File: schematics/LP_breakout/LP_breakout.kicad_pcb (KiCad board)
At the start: 2 copper layers, 39.8 x 69.8 mm, 8 parts, among them J1 RJ45, J2 Conn_01x03_Socket, J3 Conn_02x04_Odd_Even, J4 Conn_02x15_Odd_Even, J5 Conn_02x02_Odd_Even, J6 Conn_01x03_Socket, J7 Conn_01x03_Socket, J8 Conn_01x03_Socket

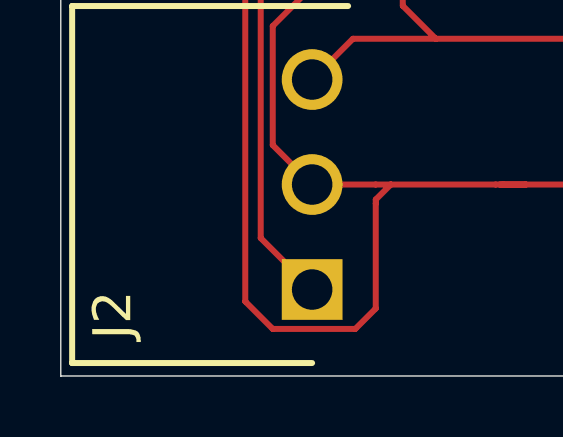
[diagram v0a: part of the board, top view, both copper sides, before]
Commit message: Updated LP Breakout for JLC
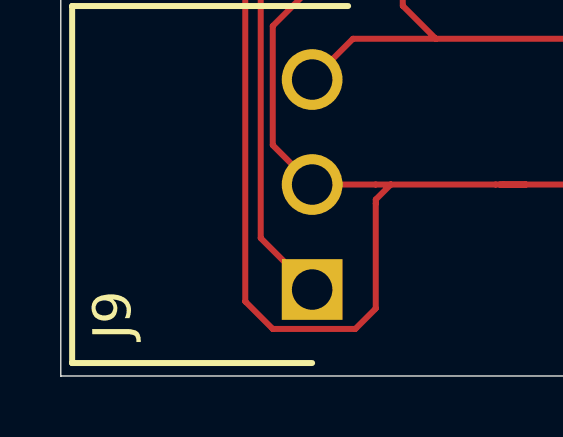
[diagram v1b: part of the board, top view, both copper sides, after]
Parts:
- renumbered J2 to J9
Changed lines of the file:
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@@
 			(drillshape 0)
 			(scaleselection 1)
-			(outputdirectory "./")
+			(outputdirectory "C:/Users/smbea/OneDrive/Personal_Files/School/Fall_2025/OATS/avena-rs/schematics/LP_breakout/JLCPCB/")
 		)
 	)
@@
 		(descr "1844223")
 		(tags "Connector")
-		(property "Reference" "J2"
+		(property "Reference" "J9"
 			(at -0.849 -6.65 90)
 			(layer "F.SilkS")

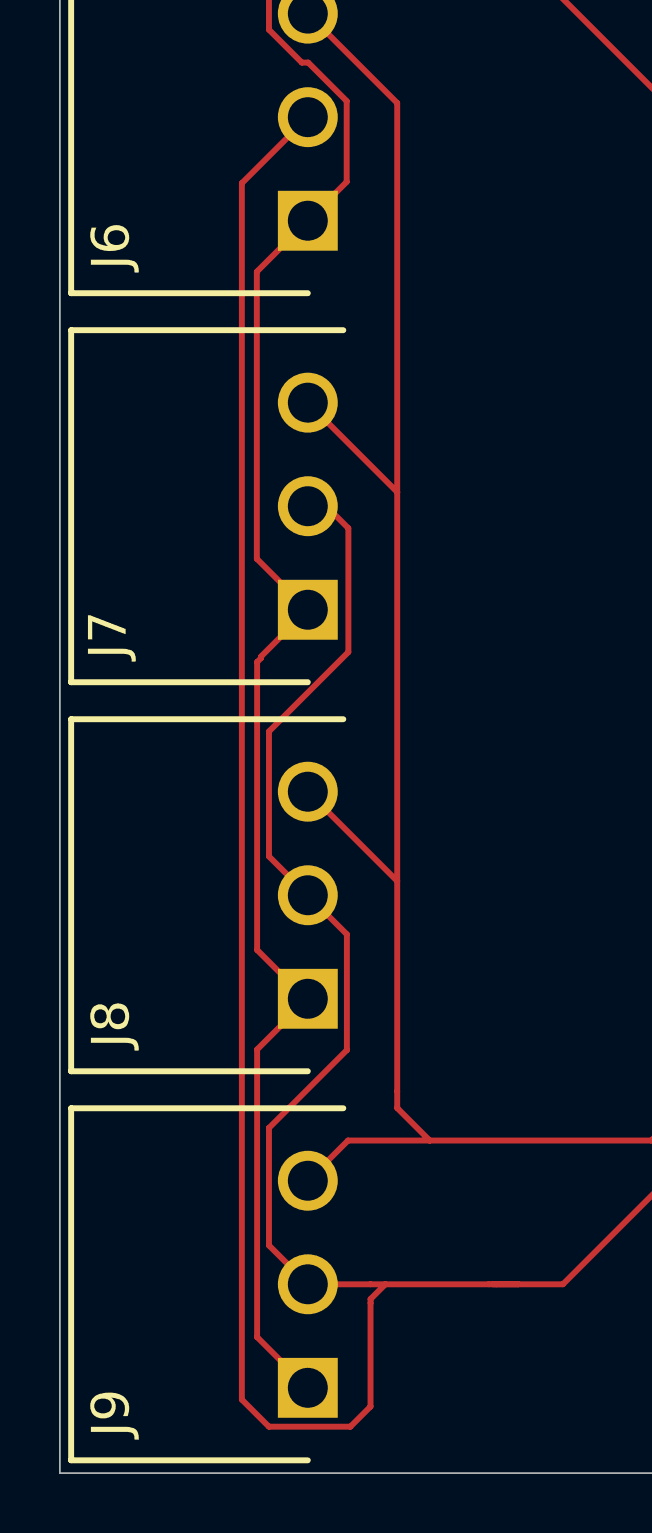
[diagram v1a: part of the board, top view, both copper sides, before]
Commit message: Update libraries to one lib for all projects
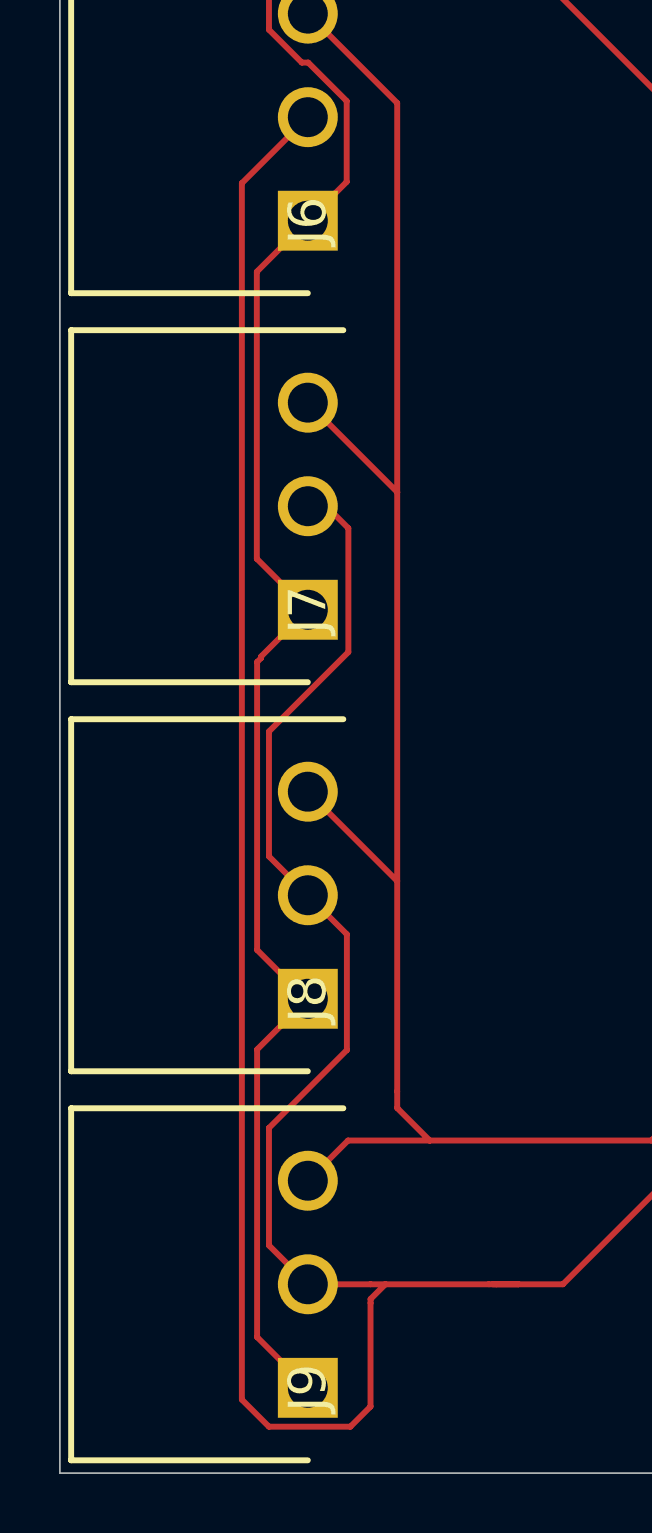
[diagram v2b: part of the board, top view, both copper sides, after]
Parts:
- J6, J7, J8, J9: footprint Library:MC1,5_3-G-3,5 -> Link_Footprints:PC-1844223
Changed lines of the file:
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@@
 	(net 41 "unconnected-(J4-Pin_15-Pad15)")
 	(net 42 "unconnected-(J4-Pin_16-Pad16)")
-	(footprint "Library:MC1,5_3-G-3,5"
+	(footprint "Link_Footprints:PC-1844223"
 		(layer "F.Cu")
 		(at 81.88 97.368 90)
@@
 		(tags "Connector")
 		(property "Reference" "J9"
-			(at -0.849 -6.65 90)
+			(at 0 0 90)
 			(layer "F.SilkS")
 			(effects
@@
 		)
 		(embedded_fonts no)
-		(model "1844223.stp"
+		(model "${KIPRJMOD}/../libraries/models/PC-1844223.stp"
 			(offset
 				(xyz 6.999999895 -1.20000003 -0.1399999985)
@@
 		)
 	)
-	(footprint "Library:MC1,5_3-G-3,5"
+	(footprint "Link_Footprints:PC-1844223"
 		(layer "F.Cu")
 		(at 81.88 71.068 90)
@@
 		(tags "Connector")
 		(property "Reference" "J7"
-			(at -0.849 -6.75 90)
+			(at 0 0 90)
 			(layer "F.SilkS")
 			(effects
@@
 		)
 		(embedded_fonts no)
-		(model "1844223.stp"
+		(model "${KIPRJMOD}/../libraries/models/PC-1844223.stp"
 			(offset
 				(xyz 6.999999895 -1.20000003 -0.1399999985)
@@
 		)
 	)
-	(footprint "Library:MC1,5_3-G-3,5"
+	(footprint "Link_Footprints:PC-1844223"
 		(layer "F.Cu")
 		(at 81.88 84.218 90)
@@
 		(tags "Connector")
 		(property "Reference" "J8"
-			(at -0.849 -6.65 90)
+			(at 0 0 90)
 			(layer "F.SilkS")
 			(effects
@@
 		)
 		(embedded_fonts no)
-		(model "1844223.stp"
+		(model "${KIPRJMOD}/../libraries/models/PC-1844223.stp"
 			(offset
 				(xyz 6.999999895 -1.20000003 -0.1399999985)
@@
 		)
 	)
-	(footprint "Library:MC1,5_3-G-3,5"
+	(footprint "Link_Footprints:PC-1844223"
 		(layer "F.Cu")
 		(at 81.88 57.918 90)
@@
 		(tags "Connector")
 		(property "Reference" "J6"
-			(at -0.849 -6.65 90)
+			(at 0 0 90)
 			(layer "F.SilkS")
 			(effects
@@
 		)
 		(embedded_fonts no)
-		(model "1844223.stp"
+		(model "${KIPRJMOD}/../libraries/models/PC-1844223.stp"
 			(offset
 				(xyz 6.999999895 -1.20000003 -0.1399999985)

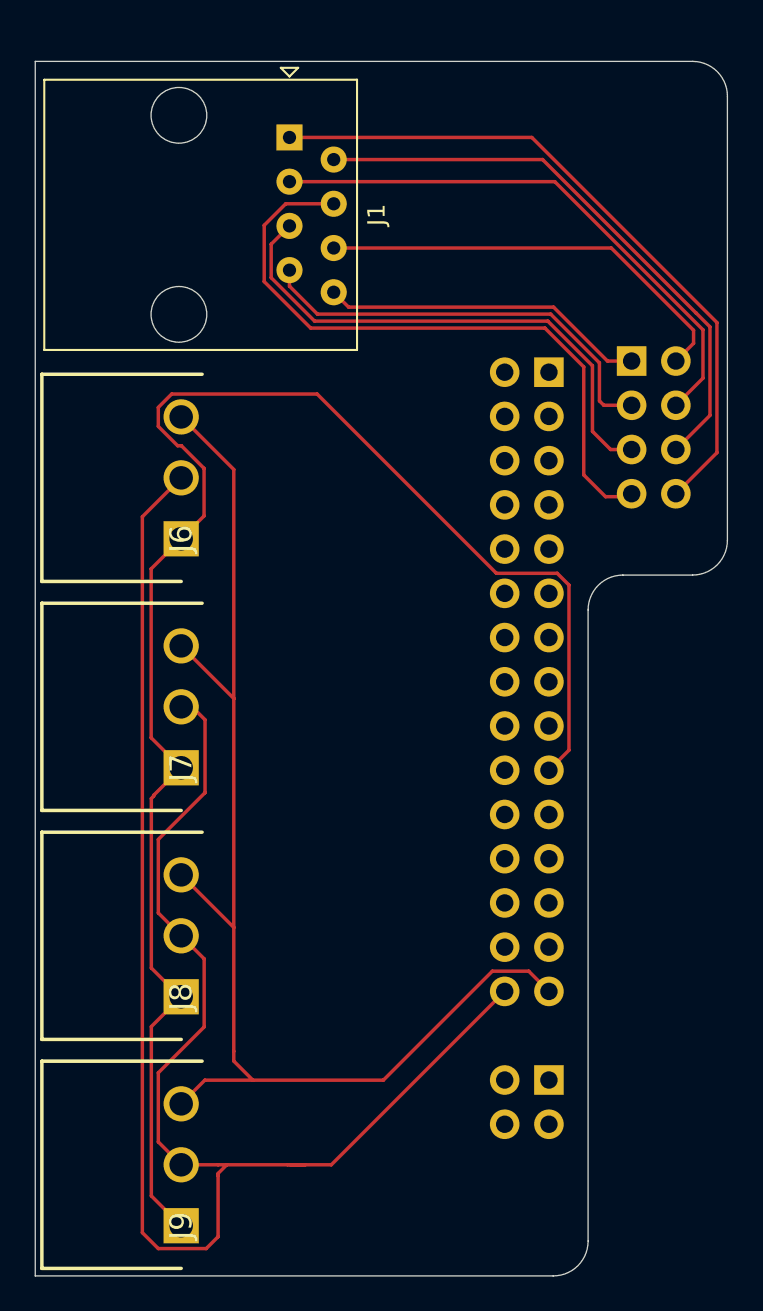
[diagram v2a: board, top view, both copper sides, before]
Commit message: update breakout board
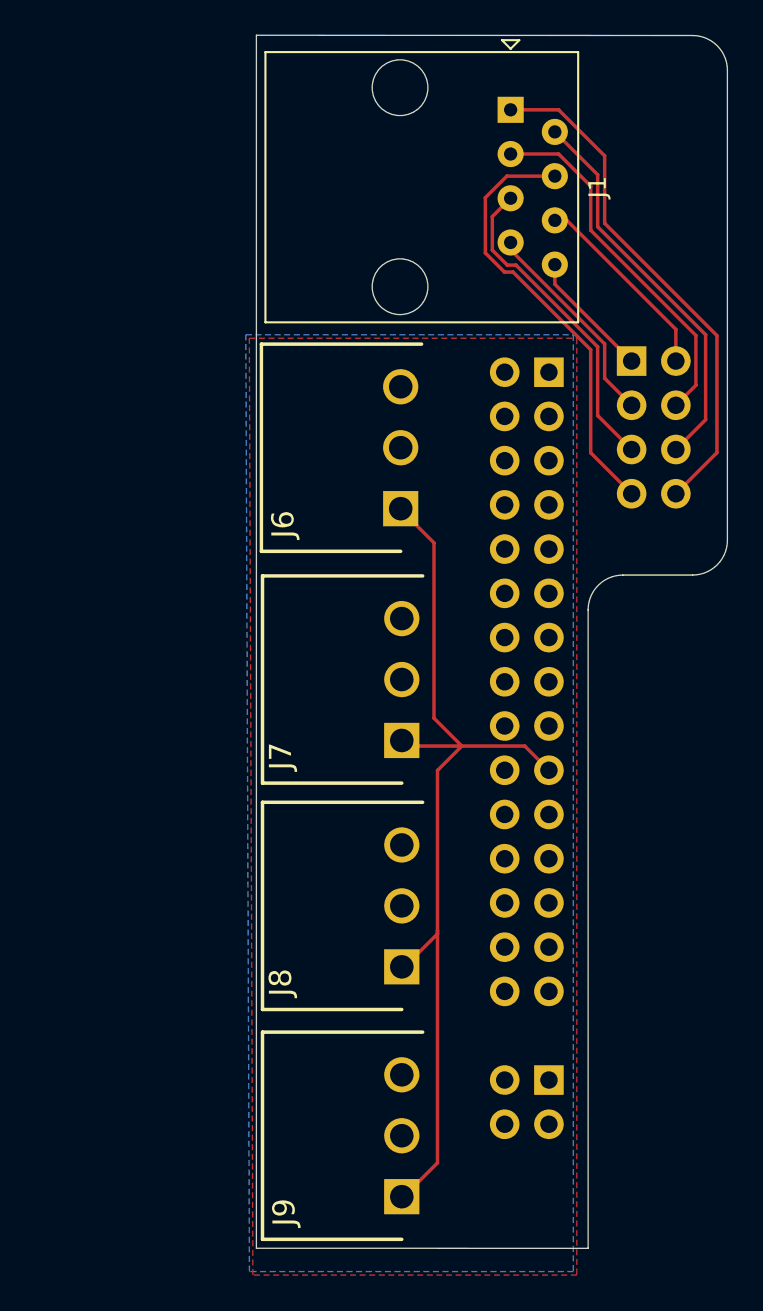
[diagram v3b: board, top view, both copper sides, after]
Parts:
- moved J7 14.2 mm to (96.0, 72.2), turned to -90 degrees
- moved J9 14.2 mm to (96.0, 98.4), turned to -90 degrees
- moved J8 14.2 mm to (96.0, 85.2), turned to -90 degrees
- moved J6 14.1 mm to (95.9, 58.9), turned to -90 degrees
- moved J1 12.8 mm to (100.8, 33.3)
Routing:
- net /SDI_GND: track 108.3 -> 0.00 mm
- net /SDI_PWR: track 73.7 -> 0.00 mm
- net /SDI_COMM: track 92.7 -> 54.5 mm
- net /LED_HDD_{+}: track 24.8 -> 11.4 mm
- net /LED_PWR_{-}: track 24.7 -> 12.2 mm
- net /BTN_PWR_{+}: track 37.7 -> 25.3 mm
- net /BTN_PWR_{-}: track 30.6 -> 18.5 mm
- net /LED_PWR_{+}: track 18.7 -> 7.37 mm
- net /LED_HDD_{-}: track 32.2 -> 20.9 mm
- net /BTN_RST_{+}: track 33.4 -> 22.5 mm
- net /BTN_RST_{-}: track 39.8 -> 29.5 mm
- added copper zone on F.Cu, net /SDI_GND
- added copper zone on B.Cu, net /SDI_PWR
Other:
- board size 39.8 x 69.8 mm -> 27 x 69.7 mm
